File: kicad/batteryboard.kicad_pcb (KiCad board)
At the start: 2 copper layers, 41.9 x 72.4 mm, 19 parts, among them U1 PANSTAMP_02, U3 DHT22, U4 MAX1724

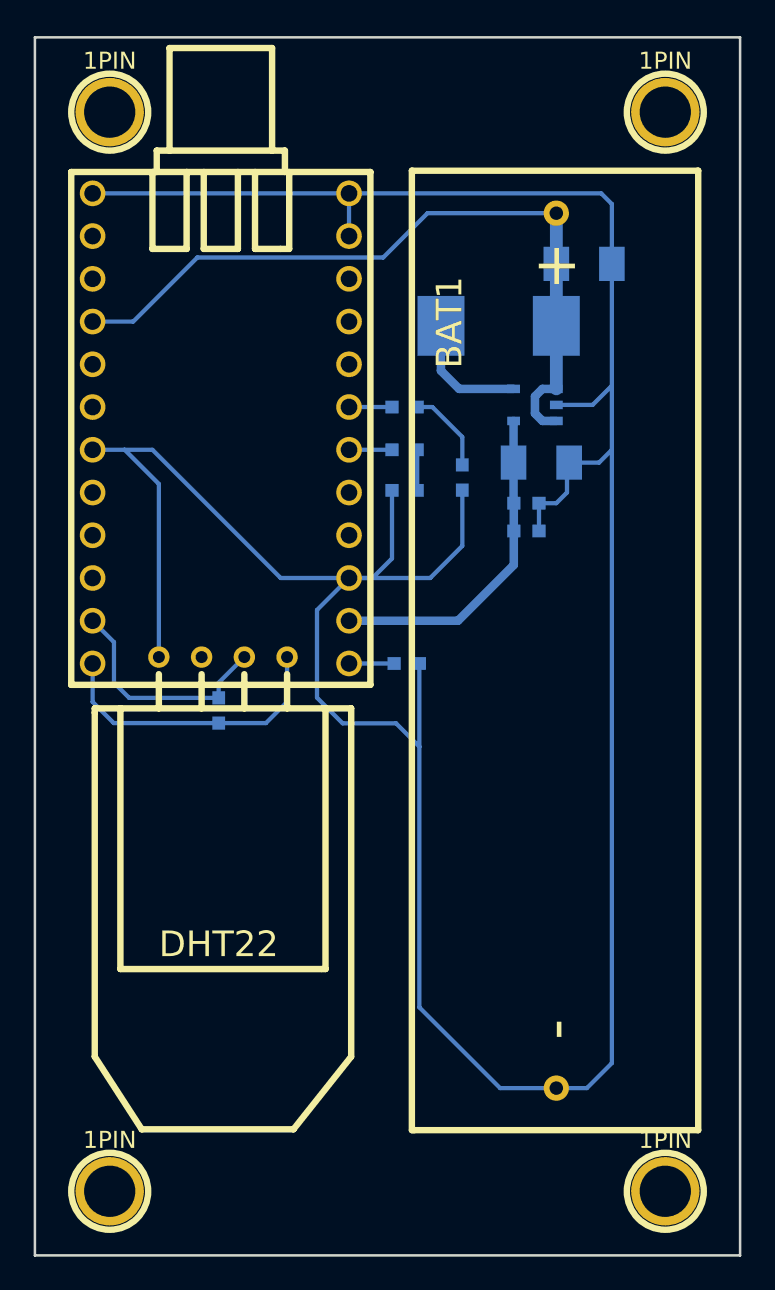
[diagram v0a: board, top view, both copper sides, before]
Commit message: change ports for sensor and battery sensing
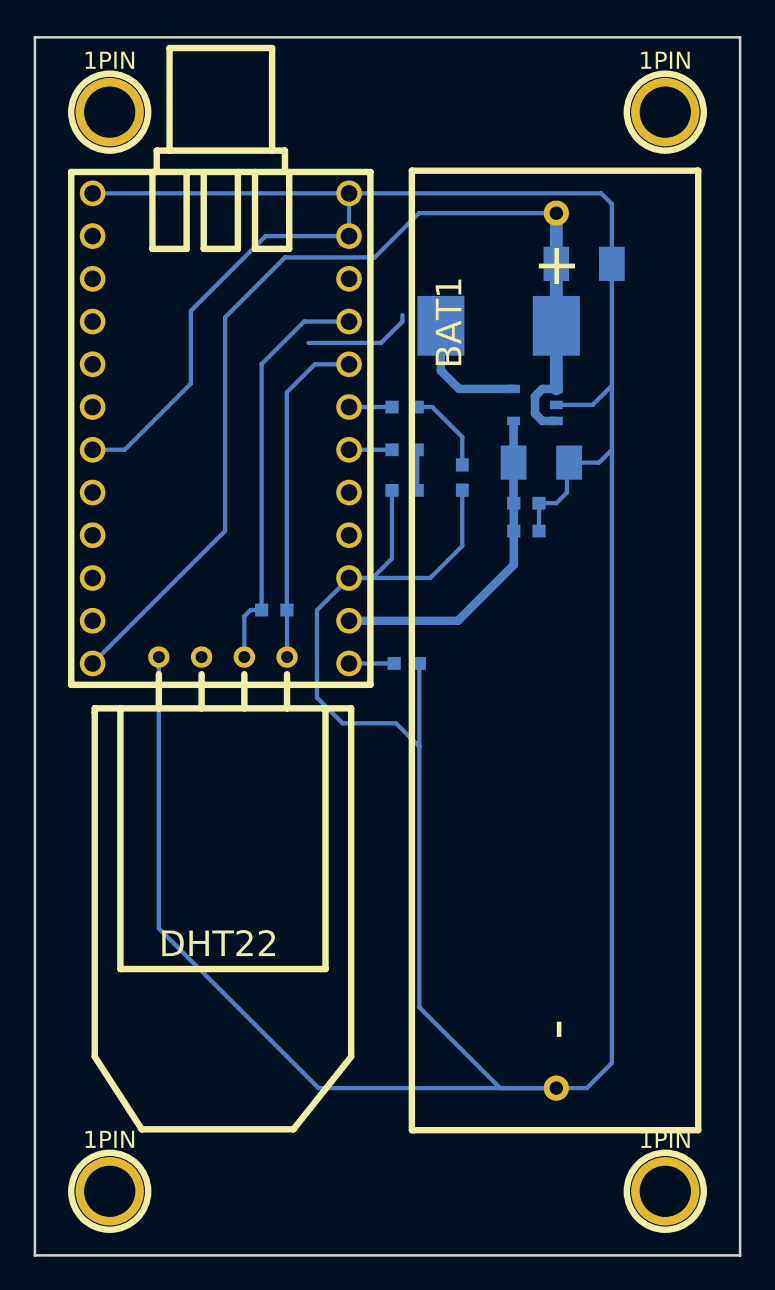
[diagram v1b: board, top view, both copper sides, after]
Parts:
- moved R3 6.82 mm to (174.2, 102.6), turned to 180 degrees
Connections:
- U1 pad 11: /A1 -> (no net)
- U1 pad 12: /A2 -> /BATTERY
- U1 pad 20: (no net) -> /A2
- U1 pad 21: (no net) -> /A1
- U1 pad 4: /BATTERY -> (no net)
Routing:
- net GND: track 195.9 -> 237.6 mm
- net /BATTERY: track 44.6 -> 60.4 mm
- net /A1: track 13.9 -> 24.5 mm
- net /A2: track 17.6 -> 20.1 mm

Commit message: reroute path for battery sensing
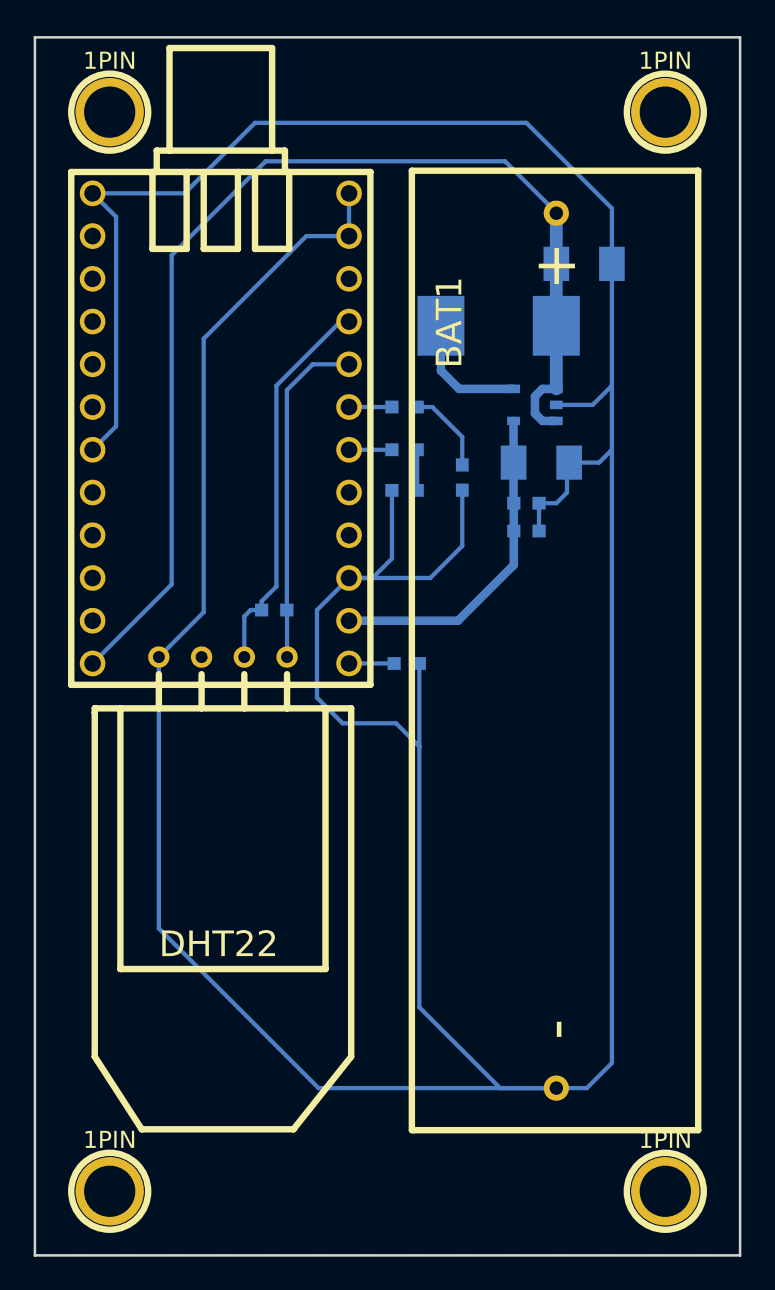
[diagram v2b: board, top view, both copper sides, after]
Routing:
- net GND: track 237.6 -> 258.9 mm
- net /BATTERY: track 60.4 -> 67.0 mm
- net /A1: track 24.5 -> 23.2 mm
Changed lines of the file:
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@@
     (thickness 1.6)
     (drawings 4)
-    (tracks 87)
+    (tracks 89)
     (zones 0)
     (modules 19)
@@
   (segment (start 188.468 96.2533) (end 188.4807 96.266) (width 0.508) (layer B.Cu) (net 1))
   (segment (start 188.468 91.3765) (end 188.468 93.853) (width 0.508) (layer B.Cu) (net 1))
-  (segment (start 173.4947 102.616) (end 173.4947 87.9983) (width 0.254) (layer B.Cu) (net 2) (status 400000))
-  (segment (start 176.022 85.471) (end 178.689 85.471) (width 0.254) (layer B.Cu) (net 2) (status 800000))
-  (segment (start 173.4947 87.9983) (end 176.022 85.471) (width 0.254) (layer B.Cu) (net 2))
+  (segment (start 173.4947 102.616) (end 173.4947 102.0953) (width 0.254) (layer B.Cu) (net 2) (status 400000))
+  (segment (start 178.181 85.471) (end 178.689 85.471) (width 0.254) (layer B.Cu) (net 2) (status C00000))
+  (segment (start 174.371 89.281) (end 178.181 85.471) (width 0.254) (layer B.Cu) (net 2) (status 800000))
+  (segment (start 174.371 101.219) (end 174.371 89.281) (width 0.254) (layer B.Cu) (net 2))
+  (segment (start 173.4947 102.0953) (end 174.371 101.219) (width 0.254) (layer B.Cu) (net 2))
   (segment (start 172.466 105.41) (end 172.466 102.997) (width 0.254) (layer B.Cu) (net 2) (status 400000))
   (segment (start 172.847 102.616) (end 173.4947 102.616) (width 0.254) (layer B.Cu) (net 2) (status 800000))
   (segment (start 172.466 102.997) (end 172.847 102.616) (width 0.254) (layer B.Cu) (net 2))
-  (segment (start 174.9933 102.616) (end 174.9933 89.6747) (width 0.254) (layer B.Cu) (net 3) (status 400000))
-  (segment (start 176.657 88.011) (end 178.689 88.011) (width 0.254) (layer B.Cu) (net 3) (status 800000))
-  (segment (start 174.9933 89.6747) (end 176.657 88.011) (width 0.254) (layer B.Cu) (net 3))
+  (segment (start 174.9933 102.616) (end 174.9933 89.5477) (width 0.254) (layer B.Cu) (net 3) (status 400000))
+  (segment (start 176.53 88.011) (end 178.689 88.011) (width 0.254) (layer B.Cu) (net 3) (status 800000))
+  (segment (start 174.9933 89.5477) (end 176.53 88.011) (width 0.254) (layer B.Cu) (net 3))
   (segment (start 175.006 105.41) (end 175.006 102.6287) (width 0.254) (layer B.Cu) (net 3) (status C00000))
   (segment (start 175.006 102.6287) (end 174.9933 102.616) (width 0.254) (layer B.Cu) (net 3) (status C00000))
-  (segment (start 191.008 79.02956) (end 182.84444 79.02956) (width 0.254) (layer B.Cu) (net 4) (status 400000))
-  (segment (start 171.323 97.917) (end 163.449 105.791) (width 0.254) (layer B.Cu) (net 4) (status 800000))
-  (segment (start 171.323 85.217) (end 171.323 97.917) (width 0.254) (layer B.Cu) (net 4))
-  (segment (start 174.879 81.661) (end 171.323 85.217) (width 0.254) (layer B.Cu) (net 4))
-  (segment (start 180.213 81.661) (end 174.879 81.661) (width 0.254) (layer B.Cu) (net 4))
-  (segment (start 182.84444 79.02956) (end 180.213 81.661) (width 0.254) (layer B.Cu) (net 4))
+  (segment (start 191.008 79.02956) (end 191.008 78.994) (width 0.254) (layer B.Cu) (net 4) (status C00000))
+  (segment (start 168.148 101.092) (end 163.449 105.791) (width 0.254) (layer B.Cu) (net 4) (status 800000))
+  (segment (start 168.148 81.534) (end 168.148 101.092) (width 0.254) (layer B.Cu) (net 4))
+  (segment (start 173.736 75.946) (end 168.148 81.534) (width 0.254) (layer B.Cu) (net 4))
+  (segment (start 187.96 75.946) (end 173.736 75.946) (width 0.254) (layer B.Cu) (net 4))
+  (segment (start 191.008 78.994) (end 187.96 75.946) (width 0.254) (layer B.Cu) (net 4) (status 400000))
   (segment (start 191.008 89.4715) (end 190.1825 89.4715) (width 0.508) (layer B.Cu) (net 4))
   (segment (start 190.1825 91.3765) (end 191.008 91.3765) (width 0.508) (layer B.Cu) (net 4))
@@
   (segment (start 181.2417 90.551) (end 178.689 90.551) (width 0.254) (layer B.Cu) (net 6))
   (segment (start 181.3687 105.791) (end 178.689 105.791) (width 0.254) (layer B.Cu) (net 7))
-  (segment (start 181.864 85.09) (end 181.864 85.471) (width 0.254) (layer B.Cu) (net 8))
-  (segment (start 180.594 86.741) (end 176.276 86.741) (width 0.254) (layer B.Cu) (net 8))
-  (segment (start 181.864 85.471) (end 180.594 86.741) (width 0.254) (layer B.Cu) (net 8))
+  (segment (start 178.689 80.391) (end 176.149 80.391) (width 0.254) (layer B.Cu) (net 8) (status 400000))
+  (segment (start 170.053 102.743) (end 167.386 105.41) (width 0.254) (layer B.Cu) (net 8) (status 800000))
+  (segment (start 170.053 86.487) (end 170.053 102.743) (width 0.254) (layer B.Cu) (net 8))
+  (segment (start 176.149 80.391) (end 170.053 86.487) (width 0.254) (layer B.Cu) (net 8))
+  (segment (start 163.449 77.851) (end 168.91 77.851) (width 0.254) (layer B.Cu) (net 8) (status 400000))
+  (segment (start 194.31 78.74) (end 194.31 82.042) (width 0.254) (layer B.Cu) (net 8) (status 800000))
+  (segment (start 189.23 73.66) (end 194.31 78.74) (width 0.254) (layer B.Cu) (net 8))
+  (segment (start 173.101 73.66) (end 189.23 73.66) (width 0.254) (layer B.Cu) (net 8))
+  (segment (start 168.91 77.851) (end 173.101 73.66) (width 0.254) (layer B.Cu) (net 8))
+  (segment (start 163.449 93.091) (end 164.846 91.694) (width 0.254) (layer B.Cu) (net 8) (status 400000))
+  (segment (start 164.846 79.248) (end 163.449 77.851) (width 0.254) (layer B.Cu) (net 8) (status 800000))
+  (segment (start 164.846 91.694) (end 164.846 79.248) (width 0.254) (layer B.Cu) (net 8))
   (segment (start 167.386 105.41) (end 167.386 121.539) (width 0.254) (layer B.Cu) (net 8) (status 400000))
+  (segment (start 167.386 121.539) (end 176.87544 131.02844) (width 0.254) (layer B.Cu) (net 8))
   (segment (start 176.87544 131.02844) (end 191.008 131.02844) (width 0.254) (layer B.Cu) (net 8) (status 800000))
-  (segment (start 167.386 121.539) (end 176.87544 131.02844) (width 0.254) (layer B.Cu) (net 8))
-  (segment (start 163.449 93.091) (end 165.354 93.091) (width 0.254) (layer B.Cu) (net 8) (status 400000))
-  (segment (start 173.736 80.391) (end 178.689 80.391) (width 0.254) (layer B.Cu) (net 8) (status 800000))
-  (segment (start 169.291 84.836) (end 173.736 80.391) (width 0.254) (layer B.Cu) (net 8))
-  (segment (start 169.291 89.154) (end 169.291 84.836) (width 0.254) (layer B.Cu) (net 8))
-  (segment (start 165.354 93.091) (end 169.291 89.154) (width 0.254) (layer B.Cu) (net 8))
   (segment (start 185.42 95.4913) (end 185.42 98.806) (width 0.254) (layer B.Cu) (net 8))
   (segment (start 183.515 100.711) (end 178.689 100.711) (width 0.254) (layer B.Cu) (net 8))
@@
   (segment (start 176.784 107.823) (end 178.308 109.347) (width 0.254) (layer B.Cu) (net 8))
   (segment (start 176.784 102.616) (end 176.784 107.823) (width 0.254) (layer B.Cu) (net 8))
-  (segment (start 194.31 82.042) (end 194.31 78.486) (width 0.254) (layer B.Cu) (net 8))
-  (segment (start 193.675 77.851) (end 178.689 77.851) (width 0.254) (layer B.Cu) (net 8))
-  (segment (start 194.31 78.486) (end 193.675 77.851) (width 0.254) (layer B.Cu) (net 8))
   (segment (start 182.8673 105.791) (end 182.8673 110.7313) (width 0.254) (layer B.Cu) (net 8))
   (segment (start 182.8673 110.7313) (end 182.8673 126.2253) (width 0.254) (layer B.Cu) (net 8))
@@
   (segment (start 189.9793 96.266) (end 189.9793 97.917) (width 0.254) (layer B.Cu) (net 8))
   (segment (start 178.689 77.851) (end 178.689 80.391) (width 0.254) (layer B.Cu) (net 8))
-  (segment (start 163.449 77.851) (end 178.689 77.851) (width 0.254) (layer B.Cu) (net 8))
   (segment (start 182.7403 93.091) (end 182.7403 95.504) (width 0.254) (layer B.Cu) (net 9))
   (segment (start 185.42 93.9927) (end 185.42 92.329) (width 0.254) (layer B.Cu) (net 10))
